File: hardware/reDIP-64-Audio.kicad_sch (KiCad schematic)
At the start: 5 parts, among them U23 SGTL5000XNLA3

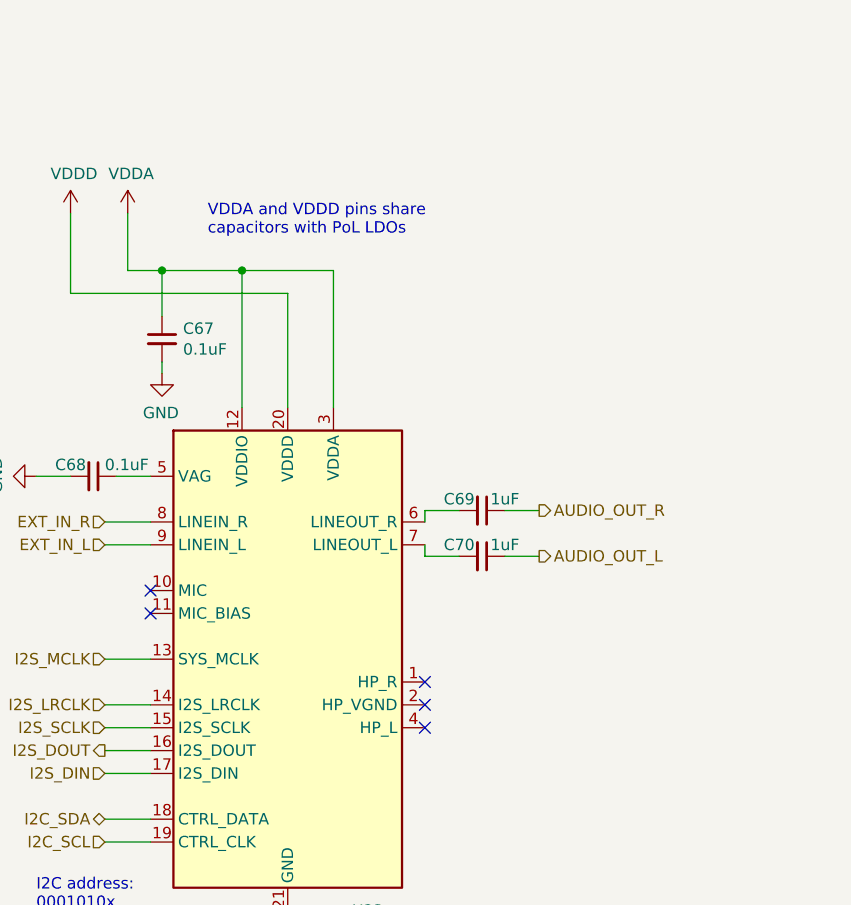
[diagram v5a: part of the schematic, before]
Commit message: Audio upgrade
* Changed from line out to headphone out with 10uF tantalum capacitors
* PTN5110 decoupling capacitor QA
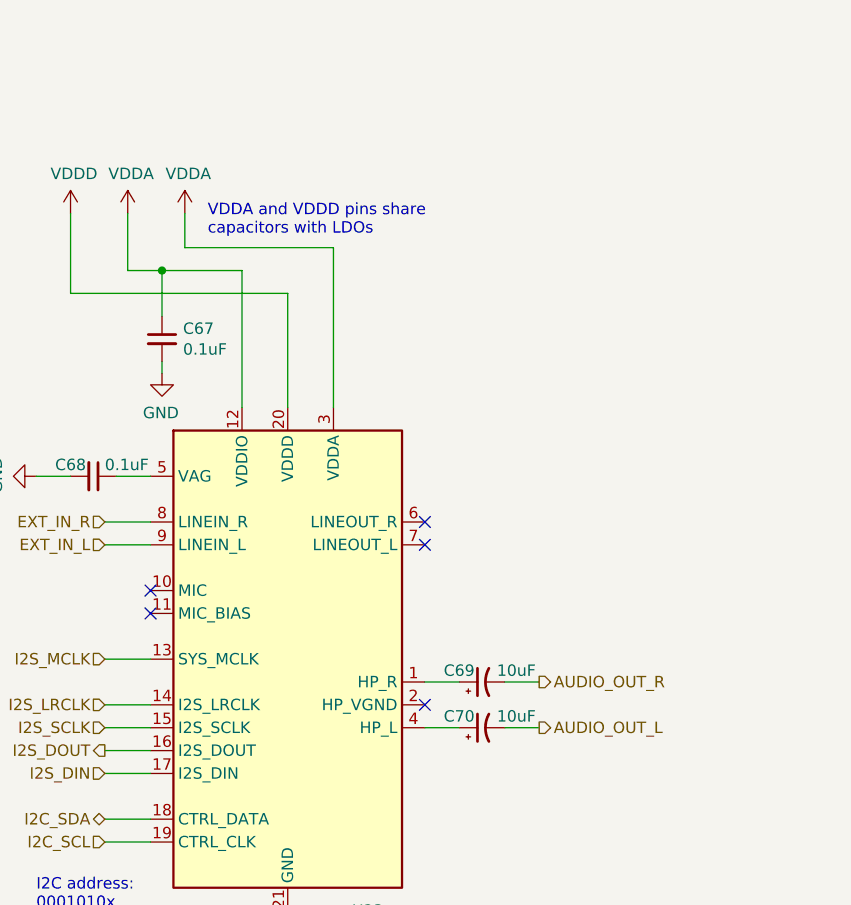
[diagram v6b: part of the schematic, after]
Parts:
- C69, C70: value 1uF -> 10uF; footprint Capacitor_SMD:C_0201_0603Metric -> Capacitor_Tantalum_SMD:CP_EIA-1608-08_AVX-J; symbol Device:C_Small -> Device:C_Polarized_Small_US; Mfg Murata -> Vishay; Notes 1.5V DC AUDIO DERATED TO 1.3uF -> 1.65V DC 1.5V AC AUDIO; PN GRM033R60J225ME01D -> TMCJ0J106MTRF
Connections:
- net AUDIO_OUT_L: now also C70.2; no longer C70.1
- net AUDIO_OUT_R: now also C69.2; no longer C69.1
- net at U23.1 (HP_R): now also C69.1
- net at U23.4 (HP_L): now also C70.1
- net at U23.6 (LINEOUT_R): no longer C69.2
- net at U23.7 (LINEOUT_L): no longer C70.2
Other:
- note added: "VDDA and VDDD pins share capacitors with LDOs"
- note removed: "VDDA and VDDD pins share capacitors with PoL LDOs"
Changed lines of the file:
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@@
   (title_block
     (title "reDIP 64")
-    (date "2022-04-14")
+    (date "2022-04-23")
     (rev "1.0")
     (company "Nimrod")
@@
     (comment 2 "Licensed under CERN-OHL-S v2 (https://ohwr.org/cern_ohl_s_v2.txt)")
   )
-  (junction (at 149.86 62.23) (diameter 0) (color 0 0 0 0)
-  )
   (junction (at 140.97 62.23) (diameter 0.9144) (color 0 0 0 0)
   )
   (no_connect (at 170.18 110.49))
-  (no_connect (at 170.18 113.03))
-  (no_connect (at 170.18 107.95))
+  (no_connect (at 170.18 92.71))
+  (no_connect (at 170.18 90.17))
   (no_connect (at 139.7 97.79))
   (no_connect (at 139.7 100.33))
@@
     (stroke (width 0) (type solid) (color 0 0 0 0))
   )
-  (wire (pts (xy 179.07 93.98) (xy 182.88 93.98))
+  (wire (pts (xy 179.07 113.03) (xy 182.88 113.03))
     (stroke (width 0) (type solid) (color 0 0 0 0))
   )
@@
     (stroke (width 0) (type solid) (color 0 0 0 0))
   )
-  (wire (pts (xy 170.18 88.9) (xy 170.18 90.17))
+  (wire (pts (xy 179.07 107.95) (xy 182.88 107.95))
+    (stroke (width 0) (type solid) (color 0 0 0 0))
+  )
+  (wire (pts (xy 139.7 90.17) (xy 134.62 90.17))
+    (stroke (width 0) (type solid) (color 0 0 0 0))
+  )
+  (wire (pts (xy 160.02 59.69) (xy 160.02 77.47))
+    (stroke (width 0) (type solid) (color 0 0 0 0))
+  )
+  (wire (pts (xy 134.62 92.71) (xy 139.7 92.71))
+    (stroke (width 0) (type solid) (color 0 0 0 0))
+  )
+  (wire (pts (xy 170.18 107.95) (xy 173.99 107.95))
+    (stroke (width 0) (type solid) (color 0 0 0 0))
+  )
+  (wire (pts (xy 154.94 133.35) (xy 154.94 139.7))
+    (stroke (width 0) (type solid) (color 0 0 0 0))
+  )
+  (wire (pts (xy 143.51 55.88) (xy 143.51 59.69))
     (stroke (width 0) (type default) (color 0 0 0 0))
   )
-  (wire (pts (xy 179.07 88.9) (xy 182.88 88.9))
-    (stroke (width 0) (type solid) (color 0 0 0 0))
-  )
-  (wire (pts (xy 139.7 90.17) (xy 134.62 90.17))
-    (stroke (width 0) (type solid) (color 0 0 0 0))
-  )
-  (wire (pts (xy 160.02 62.23) (xy 160.02 77.47))
-    (stroke (width 0) (type solid) (color 0 0 0 0))
-  )
-  (wire (pts (xy 134.62 92.71) (xy 139.7 92.71))
-    (stroke (width 0) (type solid) (color 0 0 0 0))
-  )
-  (wire (pts (xy 170.18 88.9) (xy 173.99 88.9))
-    (stroke (width 0) (type solid) (color 0 0 0 0))
-  )
-  (wire (pts (xy 154.94 133.35) (xy 154.94 139.7))
-    (stroke (width 0) (type solid) (color 0 0 0 0))
-  )
   (wire (pts (xy 130.81 55.88) (xy 130.81 64.77))
     (stroke (width 0) (type solid) (color 0 0 0 0))
@@
     (stroke (width 0) (type solid) (color 0 0 0 0))
   )
+  (wire (pts (xy 143.51 59.69) (xy 160.02 59.69))
+    (stroke (width 0) (type default) (color 0 0 0 0))
+  )
   (wire (pts (xy 154.94 64.77) (xy 154.94 77.47))
     (stroke (width 0) (type solid) (color 0 0 0 0))
   )
-  (wire (pts (xy 149.86 62.23) (xy 160.02 62.23))
-    (stroke (width 0) (type default) (color 0 0 0 0))
-  )
   (wire (pts (xy 134.62 105.41) (xy 139.7 105.41))
     (stroke (width 0) (type solid) (color 0 0 0 0))
@@
     (stroke (width 0) (type solid) (color 0 0 0 0))
   )
-  (wire (pts (xy 170.18 93.98) (xy 173.99 93.98))
+  (wire (pts (xy 170.18 113.03) (xy 173.99 113.03))
     (stroke (width 0) (type solid) (color 0 0 0 0))
   )
@@
     (stroke (width 0) (type solid) (color 0 0 0 0))
   )
-  (wire (pts (xy 170.18 92.71) (xy 170.18 93.98))
-    (stroke (width 0) (type default) (color 0 0 0 0))
-  )
   (wire (pts (xy 134.62 118.11) (xy 139.7 118.11))
     (stroke (width 0) (type solid) (color 0 0 0 0))
@@
     (stroke (width 0) (type solid) (color 0 0 0 0))
   )
-  (text "VDDA and VDDD pins share\ncapacitors with PoL LDOs" (at 146.05 58.42 0)
+  (text "VDDA and VDDD pins share\ncapacitors with LDOs" (at 146.05 58.42 0)
     (effects (font (size 1.27 1.27)) (justify left bottom))
   )
@@
     (effects (font (size 1.27 1.27)) (justify right))
   )
-  (hierarchical_label "AUDIO_OUT_L" (shape output) (at 182.88 93.98 0)
+  (hierarchical_label "AUDIO_OUT_L" (shape output) (at 182.88 113.03 0)
     (effects (font (size 1.27 1.27)) (justify left))
   )
@@
     (effects (font (size 1.27 1.27)) (justify right))
   )
-  (hierarchical_label "AUDIO_OUT_R" (shape output) (at 182.88 88.9 0)
+  (hierarchical_label "AUDIO_OUT_R" (shape output) (at 182.88 107.95 0)
     (effects (font (size 1.27 1.27)) (justify left))
   )
@@
   (symbol (lib_id "power:GND") (at 154.94 139.7 0) (mirror y) (unit 1)
     (in_bom yes) (on_board yes)
-    (property "Reference" "#PWR0164" (id 0) (at 154.94 146.05 0)
+    (property "Reference" "#PWR0165" (id 0) (at 154.94 146.05 0)
       (effects (font (size 1.27 1.27)) hide)
     )
@@
     (pin "2")
   )
-  (symbol (lib_id "Device:C_Small") (at 176.53 88.9 270) (unit 1)
-    (in_bom yes) (on_board yes)
-    (property "Reference" "C69" (id 0) (at 173.99 87.63 90))
-    (property "Value" "1uF" (id 1) (at 179.07 87.63 90))
-    (property "Footprint" "Capacitor_SMD:C_0201_0603Metric" (id 2) (at 176.53 88.9 0)
-      (effects (font (size 1.27 1.27)) hide)
-    )
-    (property "Datasheet" "https://www.murata.com/products/productdetail.aspx?partno=GRM033R60J225ME01D" (id 3) (at 176.53 88.9 0)
-      (effects (font (size 1.27 1.27)) hide)
-    )
-    (property "Mfg" "Murata" (id 4) (at 176.53 88.9 0)
-      (effects (font (size 1.27 1.27)) hide)
-    )
-    (property "PN" "GRM033R60J225ME01D" (id 5) (at 176.53 88.9 0)
-      (effects (font (size 1.27 1.27)) hide)
-    )
-    (property "Description" "CAP CER 2.2uF 6.3V 20% X5R 0201" (id 6) (at 176.53 88.9 0)
-      (effects (font (size 1.27 1.27)) hide)
-    )
-    (property "Notes" "1.5V DC AUDIO DERATED TO 1.3uF" (id 7) (at 176.53 88.9 0)
-      (effects (font (size 1.27 1.27)) hide)
-    )
-    (pin "1")
-    (pin "2")
-  )
-  (symbol (lib_id "Device:C_Small") (at 176.53 93.98 270) (unit 1)
-    (in_bom yes) (on_board yes)
-    (property "Reference" "C70" (id 0) (at 173.99 92.71 90))
-    (property "Value" "1uF" (id 1) (at 179.07 92.71 90))
-    (property "Footprint" "Capacitor_SMD:C_0201_0603Metric" (id 2) (at 176.53 93.98 0)
-      (effects (font (size 1.27 1.27)) hide)
-    )
-    (property "Datasheet" "https://www.murata.com/products/productdetail.aspx?partno=GRM033R60J225ME01D" (id 3) (at 176.53 93.98 0)
-      (effects (font (size 1.27 1.27)) hide)
-    )
-    (property "Mfg" "Murata" (id 4) (at 176.53 93.98 0)
-      (effects (font (size 1.27 1.27)) hide)
-    )
-    (property "PN" "GRM033R60J225ME01D" (id 5) (at 176.53 93.98 0)
-      (effects (font (size 1.27 1.27)) hide)
-    )
-    (property "Description" "CAP CER 2.2uF 6.3V 20% X5R 0201" (id 6) (at 176.53 93.98 0)
-      (effects (font (size 1.27 1.27)) hide)
-    )
-    (property "Notes" "1.5V DC AUDIO DERATED TO 1.3uF" (id 7) (at 176.53 93.98 0)
+  (symbol (lib_id "Device:C_Polarized_Small_US") (at 176.53 107.95 90) (unit 1)
+    (in_bom yes) (on_board yes)
+    (property "Reference" "C69" (id 0) (at 173.99 106.68 90))
+    (property "Value" "10uF" (id 1) (at 180.34 106.68 90))
+    (property "Footprint" "Capacitor_Tantalum_SMD:CP_EIA-1608-08_AVX-J" (id 2) (at 176.53 107.95 0)
+      (effects (font (size 1.27 1.27)) hide)
+    )
+    (property "Datasheet" "https://www.vishay.com/docs/40176/tmcj.pdf" (id 3) (at 176.53 107.95 0)
+      (effects (font (size 1.27 1.27)) hide)
+    )
+    (property "Mfg" "Vishay" (id 4) (at 176.53 107.95 0)
+      (effects (font (size 1.27 1.27)) hide)
+    )
+    (property "PN" "TMCJ0J106MTRF" (id 5) (at 176.53 107.95 0)
+      (effects (font (size 1.27 1.27)) hide)
+    )
+    (property "Description" "CAP TANT 10uF 6.3V 20% 0603" (id 6) (at 176.53 107.95 0)
+      (effects (font (size 1.27 1.27)) hide)
+    )
+    (property "Notes" "1.65V DC 1.5V AC AUDIO" (id 7) (at 176.53 107.95 0)
+      (effects (font (size 1.27 1.27)) hide)
+    )
+    (pin "1")
+    (pin "2")
+  )
+  (symbol (lib_id "Device:C_Polarized_Small_US") (at 176.53 113.03 90) (unit 1)
+    (in_bom yes) (on_board yes)
+    (property "Reference" "C70" (id 0) (at 173.99 111.76 90))
+    (property "Value" "10uF" (id 1) (at 180.34 111.76 90))
+    (property "Footprint" "Capacitor_Tantalum_SMD:CP_EIA-1608-08_AVX-J" (id 2) (at 176.53 113.03 0)
+      (effects (font (size 1.27 1.27)) hide)
+    )
+    (property "Datasheet" "https://www.vishay.com/docs/40176/tmcj.pdf" (id 3) (at 176.53 113.03 0)
+      (effects (font (size 1.27 1.27)) hide)
+    )
+    (property "Mfg" "Vishay" (id 4) (at 176.53 113.03 0)
+      (effects (font (size 1.27 1.27)) hide)
+    )
+    (property "PN" "TMCJ0J106MTRF" (id 5) (at 176.53 113.03 0)
+      (effects (font (size 1.27 1.27)) hide)
+    )
+    (property "Description" "CAP TANT 10uF 6.3V 20% 0603" (id 6) (at 176.53 113.03 0)
+      (effects (font (size 1.27 1.27)) hide)
+    )
+    (property "Notes" "1.65V DC 1.5V AC AUDIO" (id 7) (at 176.53 113.03 0)
       (effects (font (size 1.27 1.27)) hide)
     )
@@
   (symbol (lib_id "power:GND") (at 140.97 73.66 0) (mirror y) (unit 1)
     (in_bom yes) (on_board yes)
-    (property "Reference" "#PWR0162" (id 0) (at 140.97 80.01 0)
+    (property "Reference" "#PWR0163" (id 0) (at 140.97 80.01 0)
       (effects (font (size 1.27 1.27)) hide)
     )
@@
   (symbol (lib_id "power:GND") (at 127 85.09 270) (mirror x) (unit 1)
     (in_bom yes) (on_board yes)
-    (property "Reference" "#PWR0163" (id 0) (at 120.65 85.09 0)
+    (property "Reference" "#PWR0164" (id 0) (at 120.65 85.09 0)
       (effects (font (size 1.27 1.27)) hide)
     )
@@
     )
   )
+  (symbol (lib_id "power:VDDA") (at 143.51 55.88 0) (unit 1)
+    (in_bom yes) (on_board yes)
+    (property "Reference" "#PWR0162" (id 0) (at 143.51 59.69 0)
+      (effects (font (size 1.27 1.27)) hide)
+    )
+    (property "Value" "VDDA" (id 1) (at 143.891 51.4858 0))
+    (property "Footprint" "" (id 2) (at 143.51 55.88 0)
+      (effects (font (size 1.27 1.27)) hide)
+    )
+    (property "Datasheet" "" (id 3) (at 143.51 55.88 0)
+      (effects (font (size 1.27 1.27)) hide)
+    )
+    (pin "1")
+  )
 )
